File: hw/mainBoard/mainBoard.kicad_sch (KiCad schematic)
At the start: 0 parts

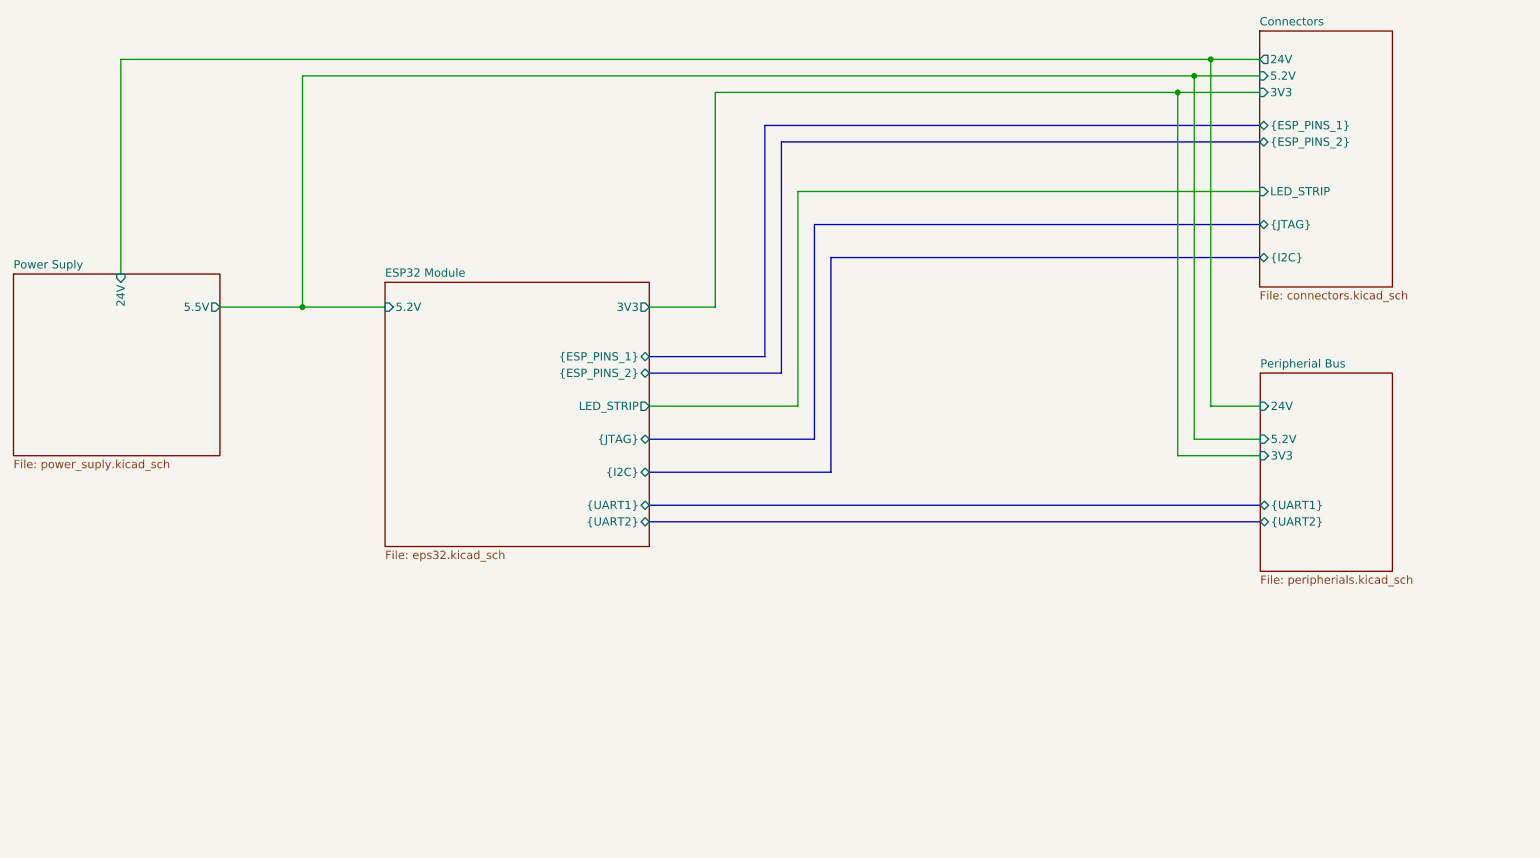
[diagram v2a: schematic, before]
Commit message: hw - changed uart2 pins, latex- ridici jednotka
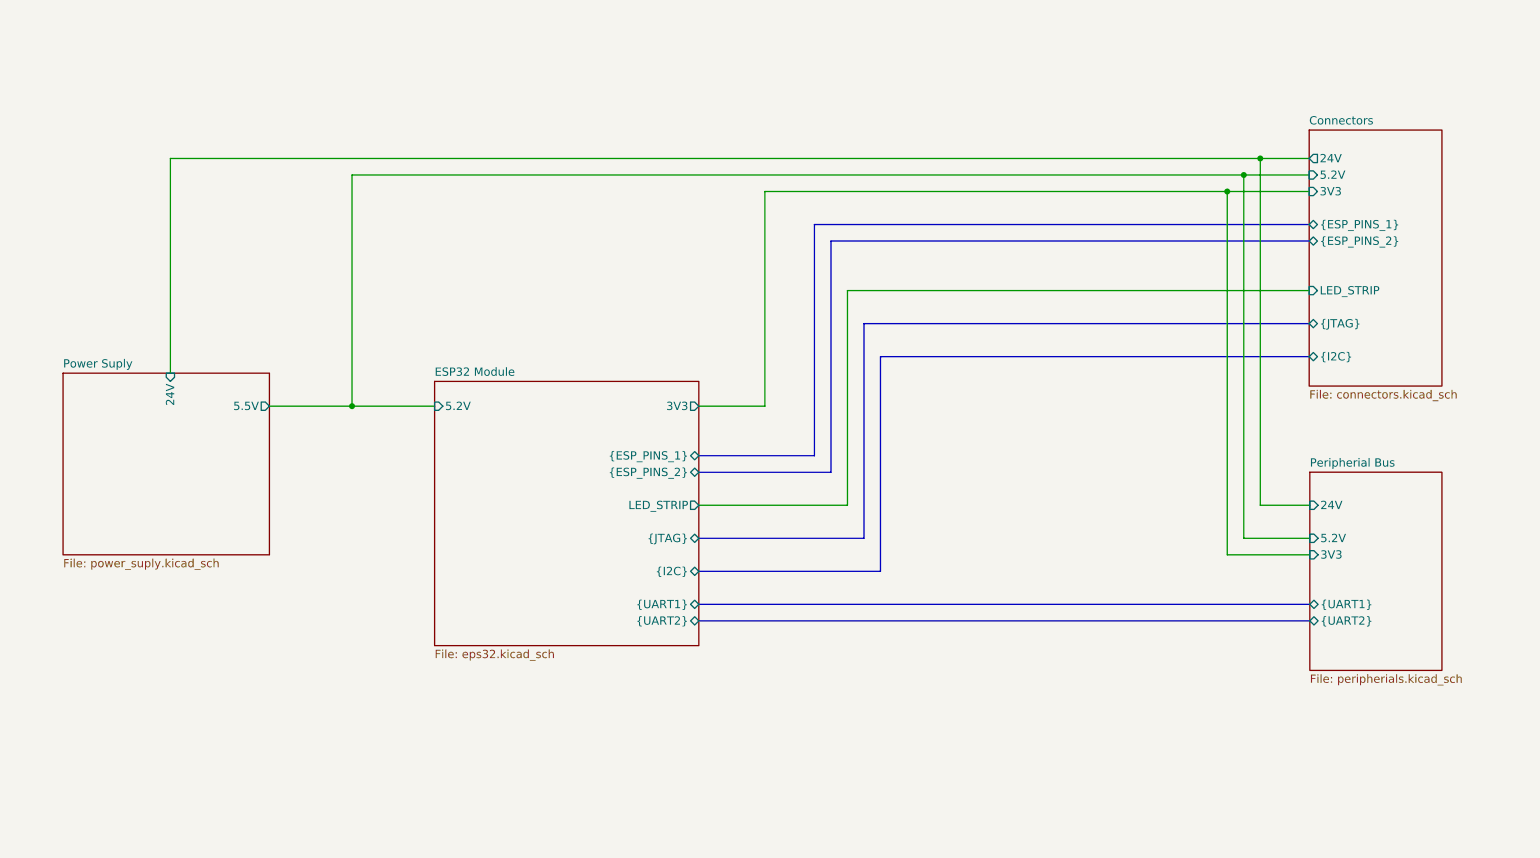
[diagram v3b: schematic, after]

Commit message: schematka
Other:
- sheet Power Suply ports: added 5.2V; removed 5.5V
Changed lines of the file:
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@@
       (effects (font (size 1.27 1.27)) (justify left top))
-    )
-    (pin "5.5V" output (at 71.12 88.9 0)
-      (effects (font (size 1.27 1.27)) (justify right))
     )
     (pin "24V" input (at 55.88 83.82 90)
       (effects (font (size 1.27 1.27)) (justify right))
     )
+    (pin "5.2V" output (at 71.12 88.9 0)
+      (effects (font (size 1.27 1.27)) (justify right))
+    )

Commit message: drawing layout
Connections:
- no-connect marks 0 -> 1
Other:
- sheet ESP32 Module ports: added {CAN}; removed {UART1}, {UART2}
- sheet Peripherial Bus ports: added {CAN}; removed {UART1}, {UART2}
- sheet Power Suply ports: added LM_POWER_GOOD; removed none
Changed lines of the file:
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@@
 (kicad_sch (version 20230121) (generator eeschema)
   (paper "A4")
+  (bus_alias "CAN" (members "CAN_RX" "CAN_TX" "CAN_STBY"))
   (junction (at 223.52 50.8) (diameter 0) (color 0 0 0 0)
   )
@@
   (junction (at 220.98 53.34) (diameter 0) (color 0 0 0 0)
   )
+  (no_connect (at 71.12 93.98))
   (wire (pts (xy 83.82 88.9) (xy 83.82 53.34))
     (stroke (width 0) (type default))
@@
   )
   (bus (pts (xy 165.1 81.28) (xy 231.0402 81.28))
-    (stroke (width 0) (type default))
-  )
-  (bus (pts (xy 137.16 121.92) (xy 231.14 121.92))
     (stroke (width 0) (type default))
   )
@@
       (effects (font (size 1.27 1.27)) (justify left))
     )
-    (pin "{UART1}" bidirectional (at 231.14 119.38 180)
-      (effects (font (size 1.27 1.27)) (justify left))
-    )
-    (pin "{UART2}" bidirectional (at 231.14 121.92 180)
+    (pin "{CAN}" bidirectional (at 231.14 119.38 180)
       (effects (font (size 1.27 1.27)) (justify left))
     )
@@
       (effects (font (size 1.27 1.27)) (justify right))
     )
-    (pin "{UART2}" bidirectional (at 137.16 121.92 0)
-      (effects (font (size 1.27 1.27)) (justify right))
-    )
-    (pin "{UART1}" bidirectional (at 137.16 119.38 0)
+    (pin "{CAN}" bidirectional (at 137.16 119.38 0)
       (effects (font (size 1.27 1.27)) (justify right))
     )
@@
       (effects (font (size 1.27 1.27)) (justify right))
     )
+    (pin "LM_POWER_GOOD" output (at 71.12 93.98 0)
+      (effects (font (size 1.27 1.27)) (justify right))
+    )

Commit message: finale bez rybicky
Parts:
- added SJ1: SolderJumper_2_Open, Jumper:SolderJumper-2_P1.3mm_Open_RoundedPad1.0x1.5mm, symbol Jumper:SolderJumper_2_Open
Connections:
- net Connectors/5.2V: now also SJ1.1 (A)
- new net ESP32 Module/5.2V: SJ1.2 (B)
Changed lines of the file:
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@@
   (junction (at 223.52 50.8) (diameter 0) (color 0 0 0 0)
   )
+  (junction (at 76.2 88.9) (diameter 0) (color 0 0 0 0)
+  )
   (junction (at 218.44 55.88) (diameter 0) (color 0 0 0 0)
-  )
-  (junction (at 83.82 88.9) (diameter 0) (color 0 0 0 0)
   )
   (junction (at 220.98 53.34) (diameter 0) (color 0 0 0 0)
   )
   (no_connect (at 71.12 93.98))
-  (wire (pts (xy 83.82 88.9) (xy 83.82 53.34))
+  (wire (pts (xy 76.2 88.9) (xy 76.2 53.34))
     (stroke (width 0) (type default))
   )
@@
     (stroke (width 0) (type default))
   )
-  (wire (pts (xy 71.12 88.9) (xy 83.82 88.9))
+  (wire (pts (xy 71.12 88.9) (xy 76.2 88.9))
     (stroke (width 0) (type default))
   )
@@
     (stroke (width 0) (type default))
   )
-  (wire (pts (xy 83.82 53.34) (xy 220.98 53.34))
+  (wire (pts (xy 76.2 53.34) (xy 220.98 53.34))
     (stroke (width 0) (type default))
   )
@@
     (stroke (width 0) (type default))
   )
-  (wire (pts (xy 83.82 88.9) (xy 96.52 88.9))
+  (wire (pts (xy 76.2 88.9) (xy 82.55 88.9))
     (stroke (width 0) (type default))
   )
   (wire (pts (xy 223.52 50.8) (xy 55.88 50.8))
+    (stroke (width 0) (type default))
+  )
+  (wire (pts (xy 90.17 88.9) (xy 96.52 88.9))
     (stroke (width 0) (type default))
   )
@@
     (stroke (width 0) (type default))
   )
+  (symbol (lib_id "Jumper:SolderJumper_2_Open") (at 86.36 88.9 0) (unit 1)
+    (in_bom yes) (on_board yes) (dnp no)
+    (property "Reference" "SJ1" (at 86.36 82.55 0)
+      (effects (font (size 1.27 1.27)))
+    )
+    (property "Value" "SolderJumper_2_Open" (at 86.36 85.09 0)
+      (effects (font (size 1.27 1.27)) hide)
+    )
+    (property "Footprint" "Jumper:SolderJumper-2_P1.3mm_Open_RoundedPad1.0x1.5mm" (at 86.36 88.9 0)
+      (effects (font (size 1.27 1.27)) hide)
+    )
+    (property "Datasheet" "~" (at 86.36 88.9 0)
+      (effects (font (size 1.27 1.27)) hide)
+    )
+    (pin "2")
+    (pin "1")
+    (instances
+      (project "mainBoard"
+        (path "/afbe4b5f-4e5c-4a12-a44b-208d158a3f7a"
+          (reference "SJ1") (unit 1)
+        )
+      )
+    )
+  )
   (sheet (at 231.14 99.06) (size 20.32 30.48) (fields_autoplaced)
